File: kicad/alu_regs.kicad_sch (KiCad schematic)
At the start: 10 parts, among them U19 SN74F377AN, U20 SN74F377AN, U21 SN74F377AN, U5 ATF22V10C-7PX, U6 ATF22V10C-7PX

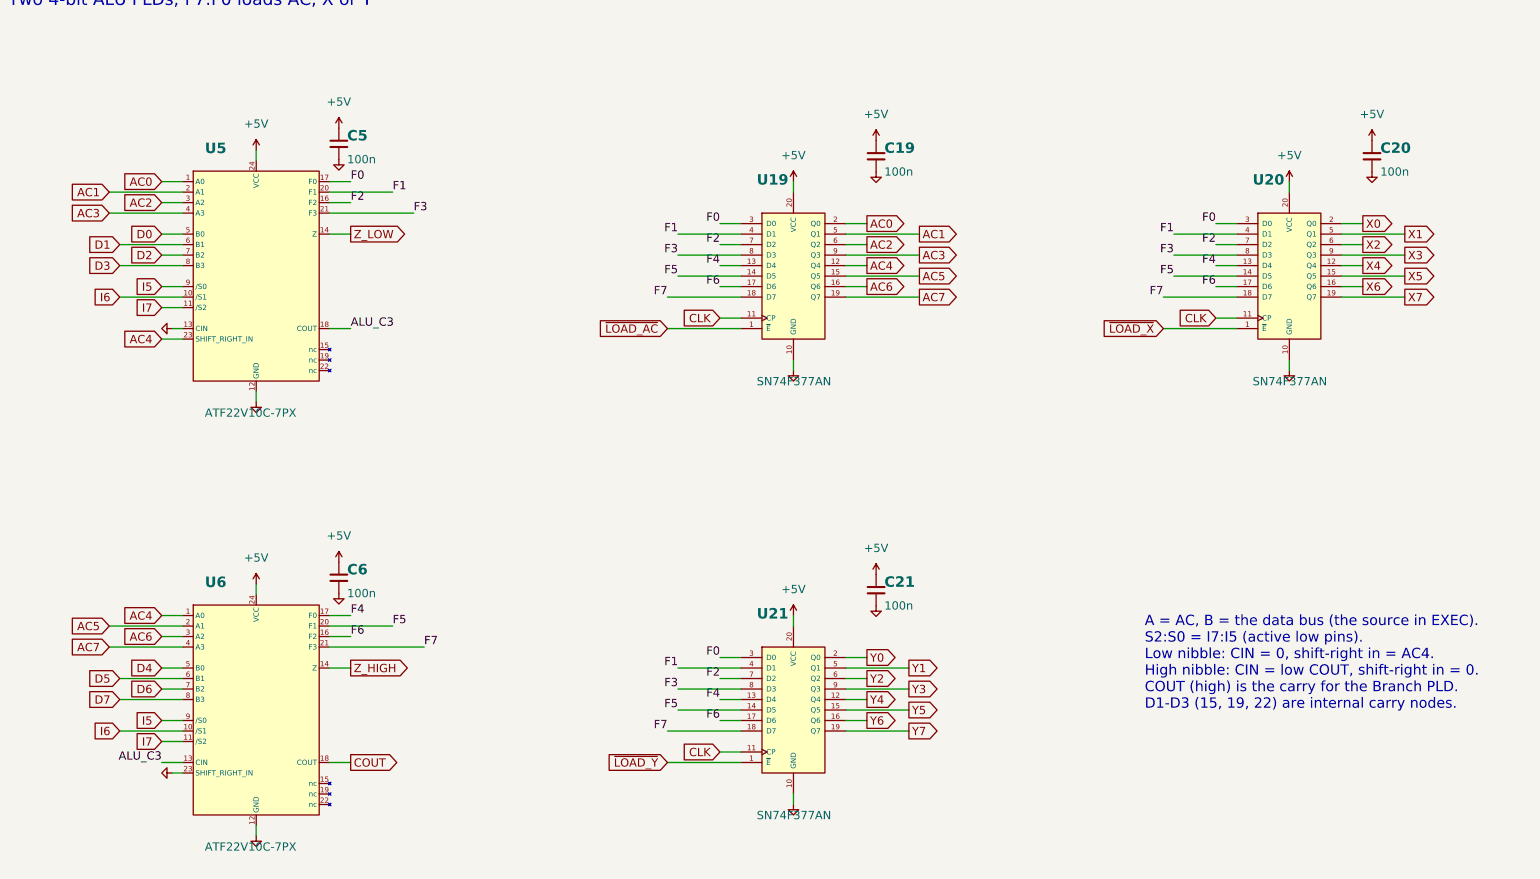
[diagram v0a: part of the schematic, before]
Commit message: KiCad schematic: wire each sheet's nets, one routed bus per bus, PLD names
A net with two or more pins on a sheet is now wired pin to pin by a small
grid router (src/scripts/kicad_route.py) instead of a label per pin.
Numbered groups (D, A, SRC, PC, ...) are drawn as one bus per sheet with
bus entries, routed between the chips and named by one bus label.  Each
PLD shows its job under its part number.  Netlist check: 0 problems.

Co-Authored-By: Claude Opus 5.5 (1M context) <noreply@anthropic.com>
Claude-Session: https://claude.ai/code/session_01L9AkLuEg13EebxDmgXsaEp
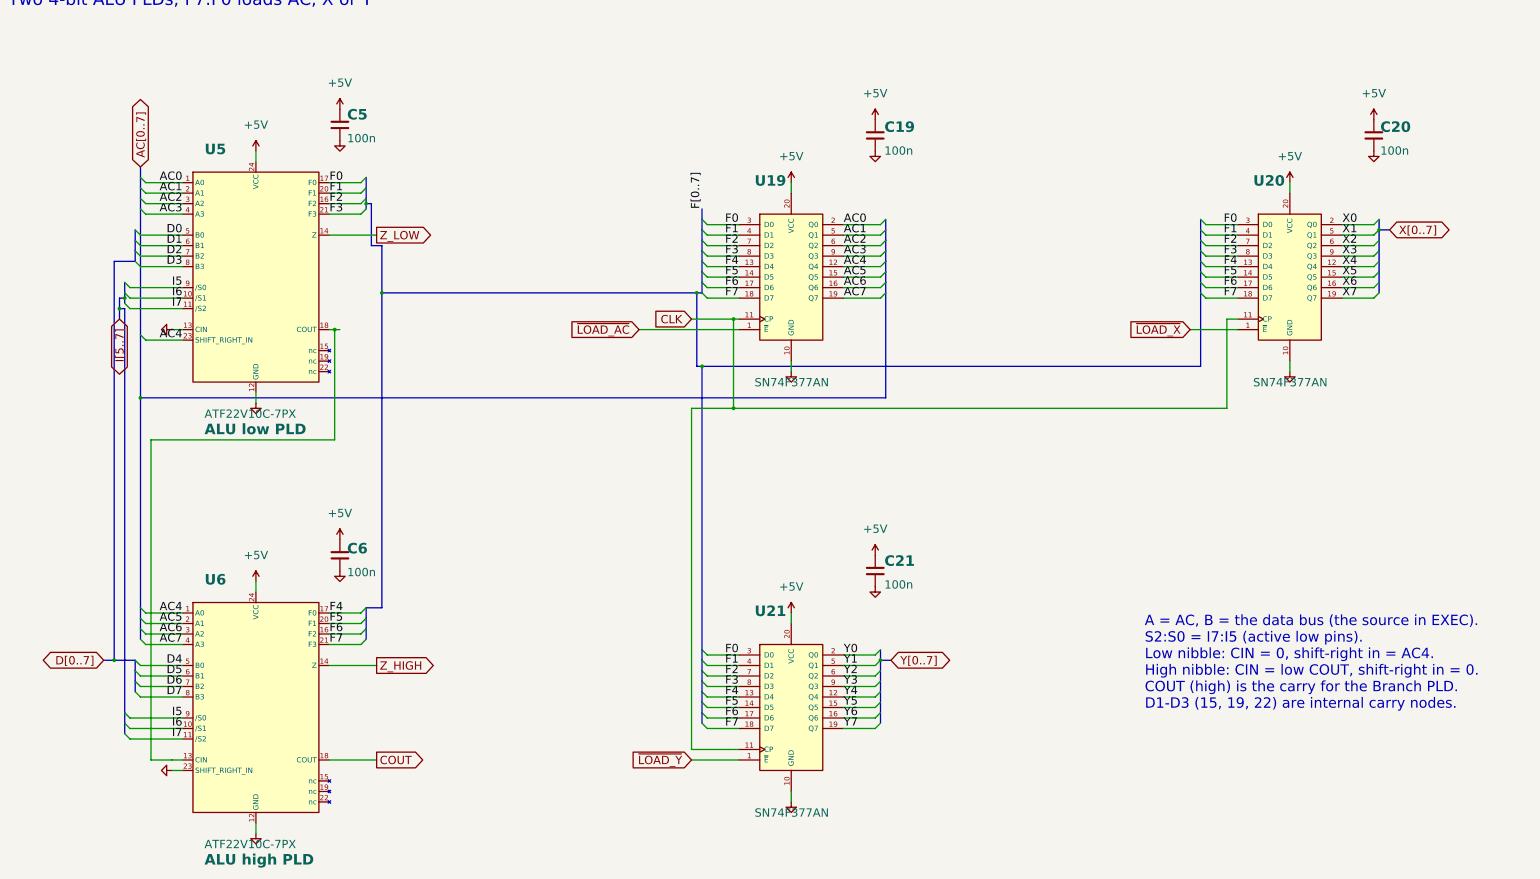
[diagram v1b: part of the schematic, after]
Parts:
- U5: Function (none) -> ALU low PLD
- U6: Function (none) -> ALU high PLD
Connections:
- net ALU_C3: no longer names the net of U5.18 (COUT), U6.13 (CIN)

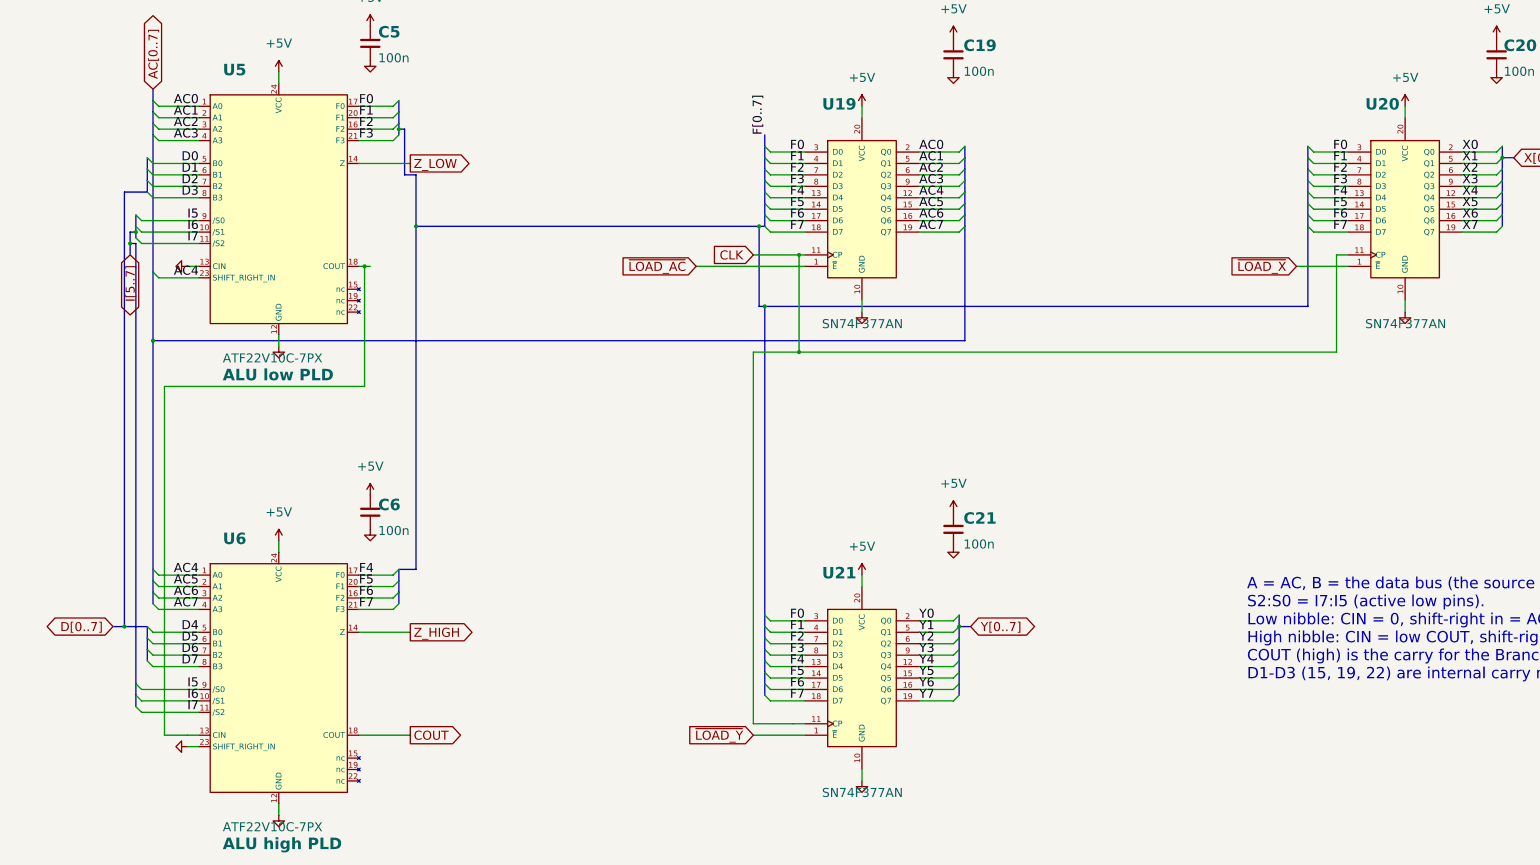
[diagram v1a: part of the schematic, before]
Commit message: Schematic: hand-placed video out sheet, larger pin text (work in progress)
The video and audio out sheet is laid out by hand like the PNG drawings:
straight PIX lines tapped onto the PIX bus, fanned RGB and DAC wires, the
ladder as a column.  KiCad's library parts are copied into placard_std with
larger pin text (gen_kicad_std.py); the PLD symbols' pin text is larger too.

Co-Authored-By: Claude Opus 5.5 (1M context) <noreply@anthropic.com>
Claude-Session: https://claude.ai/code/session_01L9AkLuEg13EebxDmgXsaEp
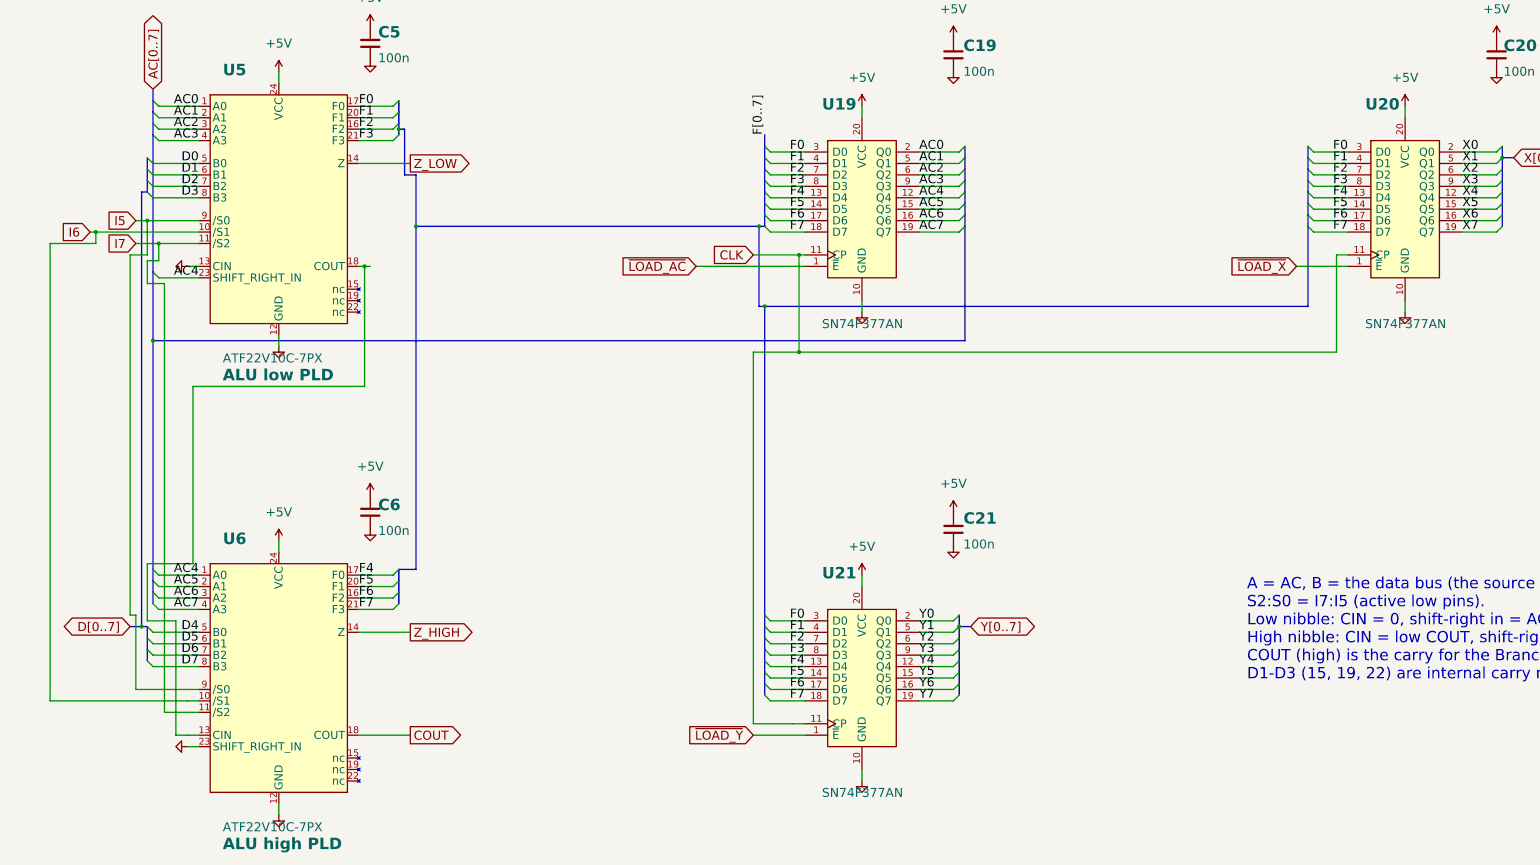
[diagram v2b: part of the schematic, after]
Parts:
- C19, C20, C21, C5, C6: symbol Device:C -> placard_std:C
- U19, U20, U21: symbol 74xx:74LS377 -> placard_std:74LS377
